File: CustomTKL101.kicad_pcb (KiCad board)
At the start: 2 copper layers, 422.3 x 131.8 mm, 223 parts, among them J1 USB4085-GF-A_REVA, SW1 SW_Push, U1 ATmega32U4-AU, Y1 16MHz

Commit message: tracing re-done
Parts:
- SW1: moved to B.Cu
- moved C5 14.6 mm to (109.0, 97.5), turned to 180 degrees
- moved R1 14.3 mm to (93.1, 85.0), turned to 90 degrees
- moved SW1 13.0 mm to (87.0, 87.1)
- moved C6 12.9 mm to (112.1, 84.5), turned to 90 degrees
- moved C4 10.2 mm to (93.7, 87.9), turned to 180 degrees
- moved R7 6.57 mm to (93.7, 92.8)
- moved R8 6.57 mm to (93.7, 94.9)
- moved R9 3.64 mm to (112.0, 96.8)
- moved C3 1.78 mm to (93.7, 90.2), turned to 180 degrees
- moved U1 1.71 mm to (104.0, 89.4)
- moved C7 1.62 mm to (98.9, 97.5)
- moved R5 0.89 mm to (80.3, 79.4)
- moved F1 0.89 mm to (84.8, 80.0)
- moved R2 0.89 mm to (87.9, 78.6)
- moved R3 0.89 mm to (82.4, 79.4)
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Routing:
- net +5V: track 38.4 -> 107.8 mm, vias 2 -> 5
- net GND: track 121.7 -> 133.8 mm, vias 3 -> 4
- net D-: track 14.2 -> 24.5 mm
- net D+: track 11.9 -> 22.1 mm
- net Net-(R1-Pad2): track 29.3 -> 22.4 mm, vias 2 -> 0
- net Net-(R7-Pad1): track 8.71 -> 4.41 mm
- net Net-(C2-Pad1): track 12.9 -> 9.58 mm, vias 2 -> 0
- net Net-(R8-Pad1): track 7.87 -> 5.17 mm
- net Net-(R9-Pad2): track 2.74 -> 3.97 mm
- net Net-(C1-Pad1): track 6.07 -> 7.06 mm
- net Net-(F1-Pad1): track 12.2 -> 11.6 mm

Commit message: changed numenter footprint
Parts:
- K_87: footprint MX_Alps_Hybrid:MX-1U-NoLED -> MX_Alps_Hybrid:MX-2U-ReversedStabilizers-NoLED
- moved D_87 12.1 mm to (479.4, 187.1), turned to 0 degrees
- turned K_87 to 270 degrees
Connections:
- K_87 pad 1: col21 -> (no net)
- K_87 pad 2: Net-(D_87-Pad2) -> (no net)

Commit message: Board Complete
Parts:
- removed K_0: KEYSW, MX_Alps_Hybrid:MX-1U-NoLED
- removed R2: 1.5k, Resistor_SMD:R_0805_2012Metric
- added MX1: MX-NoLED, MX_Alps_Hybrid:MX-1U-NoLED, F.Cu at (126.9, 83.3)
- D1: renamed from D_0; value D -> D_Small
- D10: renamed from D_9; value D -> D_Small
- D100: renamed from D_100; value D -> D_Small
- D101: renamed from D_87; value D -> D_Small
- D11: renamed from D_10; value D -> D_Small
- D12: renamed from D_11; value D -> D_Small
- D13: renamed from D_12; value D -> D_Small
- D14: renamed from D_13; value D -> D_Small
- D15: renamed from D_14; value D -> D_Small
- D16: renamed from D_15; value D -> D_Small
- D17: renamed from D_16; value D -> D_Small
- D18: renamed from D_17; value D -> D_Small
- D19: renamed from D_18; value D -> D_Small
- D2: renamed from D_1; value D -> D_Small
- D20: renamed from D_19; value D -> D_Small
- D21: renamed from D_20; value D -> D_Small
- D22: renamed from D_21; value D -> D_Small
- D23: renamed from D_22; value D -> D_Small
- D24: renamed from D_23; value D -> D_Small
- D25: renamed from D_24; value D -> D_Small
- D26: renamed from D_25; value D -> D_Small
- D27: renamed from D_26; value D -> D_Small
- D28: renamed from D_27; value D -> D_Small
- D29: renamed from D_28; value D -> D_Small
- D3: renamed from D_2; value D -> D_Small
- D30: renamed from D_29; value D -> D_Small
- D31: renamed from D_30; value D -> D_Small
- D32: renamed from D_31; value D -> D_Small
- D33: renamed from D_32; value D -> D_Small
- D34: renamed from D_33; value D -> D_Small
- D35: renamed from D_34; value D -> D_Small
- D36: renamed from D_35; value D -> D_Small
- D37: renamed from D_36; value D -> D_Small
- D38: renamed from D_37; value D -> D_Small
- D39: renamed from D_38; value D -> D_Small
- D4: renamed from D_3; value D -> D_Small
- D40: renamed from D_39; value D -> D_Small
- D41: renamed from D_40; value D -> D_Small
- D42: renamed from D_41; value D -> D_Small
- D43: renamed from D_42; value D -> D_Small
- D44: renamed from D_43; value D -> D_Small
- D45: renamed from D_44; value D -> D_Small
- D46: renamed from D_45; value D -> D_Small
- D47: renamed from D_46; value D -> D_Small
- D48: renamed from D_47; value D -> D_Small
- D49: renamed from D_48; value D -> D_Small
- D5: renamed from D_4; value D -> D_Small
- D50: renamed from D_49; value D -> D_Small
- D51: renamed from D_50; value D -> D_Small
- D52: renamed from D_51; value D -> D_Small
- D53: renamed from D_52; value D -> D_Small
- D54: renamed from D_53; value D -> D_Small
- D55: renamed from D_54; value D -> D_Small
- D56: renamed from D_55; value D -> D_Small
- D57: renamed from D_56; value D -> D_Small
- D58: renamed from D_57; value D -> D_Small
- D59: renamed from D_58; value D -> D_Small
- D6: renamed from D_5; value D -> D_Small
- D60: renamed from D_59; value D -> D_Small
- D61: renamed from D_60; value D -> D_Small
- D62: renamed from D_61; value D -> D_Small
- D63: renamed from D_62; value D -> D_Small
- D64: renamed from D_63; value D -> D_Small
- D65: renamed from D_64; value D -> D_Small
- D66: renamed from D_65; value D -> D_Small
- D67: renamed from D_66; value D -> D_Small
- D68: renamed from D_67; value D -> D_Small
- D69: renamed from D_68; value D -> D_Small
- D7: renamed from D_6; value D -> D_Small
- D70: renamed from D_69; value D -> D_Small
- D71: renamed from D_70; value D -> D_Small
- D72: renamed from D_71; value D -> D_Small
- D73: renamed from D_72; value D -> D_Small
- D74: renamed from D_73; value D -> D_Small
- D75: renamed from D_74; value D -> D_Small
- D76: renamed from D_75; value D -> D_Small
- D77: renamed from D_76; value D -> D_Small
- D78: renamed from D_77; value D -> D_Small
- D79: renamed from D_78; value D -> D_Small
- D8: renamed from D_7; value D -> D_Small
- D80: renamed from D_79; value D -> D_Small
- D81: renamed from D_80; value D -> D_Small
- D82: renamed from D_81; value D -> D_Small
- D83: renamed from D_82; value D -> D_Small
- D84: renamed from D_83; value D -> D_Small
- D85: renamed from D_84; value D -> D_Small
- D86: renamed from D_85; value D -> D_Small
- D87: renamed from D_86; value D -> D_Small
- D88: renamed from D_88; value D -> D_Small
- D89: renamed from D_89; value D -> D_Small
- D9: renamed from D_8; value D -> D_Small
- D90: renamed from D_90; value D -> D_Small
- D91: renamed from D_91; value D -> D_Small
- D92: renamed from D_92; value D -> D_Small
- D93: renamed from D_93; value D -> D_Small
- D94: renamed from D_94; value D -> D_Small
- D95: renamed from D_95; value D -> D_Small
- D96: renamed from D_96; value D -> D_Small
- D97: renamed from D_97; value D -> D_Small
- D98: renamed from D_98; value D -> D_Small
- D99: renamed from D_99; value D -> D_Small
- MX10: renamed from K_9; value KEYSW -> MX-NoLED
- MX100: renamed from K_100; value KEYSW -> MX-NoLED
- MX101: renamed from K_87; value KEYSW -> MX-NoLED; footprint MX_Alps_Hybrid:MX-2U-ReversedStabilizers-NoLED -> MX_Alps_Hybrid:MX-1U-NoLED
- MX11: renamed from K_10; value KEYSW -> MX-NoLED
- MX12: renamed from K_11; value KEYSW -> MX-NoLED
- MX13: renamed from K_12; value KEYSW -> MX-NoLED
- MX14: renamed from K_13; value KEYSW -> MX-NoLED
- MX15: renamed from K_14; value KEYSW -> MX-NoLED
- MX16: renamed from K_15; value KEYSW -> MX-NoLED
- MX17: renamed from K_16; value KEYSW -> MX-NoLED
- MX18: renamed from K_17; value KEYSW -> MX-NoLED
- MX19: renamed from K_18; value KEYSW -> MX-NoLED
- MX2: renamed from K_1; value KEYSW -> MX-NoLED
- MX20: renamed from K_19; value KEYSW -> MX-NoLED
- MX21: renamed from K_20; value KEYSW -> MX-NoLED
- MX22: renamed from K_21; value KEYSW -> MX-NoLED
- MX23: renamed from K_22; value KEYSW -> MX-NoLED
- MX24: renamed from K_23; value KEYSW -> MX-NoLED
- MX25: renamed from K_24; value KEYSW -> MX-NoLED
- MX26: renamed from K_25; value KEYSW -> MX-NoLED
- MX27: renamed from K_26; value KEYSW -> MX-NoLED
- MX28: renamed from K_27; value KEYSW -> MX-NoLED
- MX29: renamed from K_28; value KEYSW -> MX-NoLED
- MX3: renamed from K_2; value KEYSW -> MX-NoLED
- MX30: renamed from K_29; value KEYSW -> MX-NoLED
- MX31: renamed from K_30; value KEYSW -> MX-NoLED
- MX32: renamed from K_31; value KEYSW -> MX-NoLED; footprint MX_Alps_Hybrid:MX-2U-NoLED -> MX_Alps_Hybrid:MX-1U-NoLED
- MX33: renamed from K_32; value KEYSW -> MX-NoLED
- MX34: renamed from K_33; value KEYSW -> MX-NoLED
- MX35: renamed from K_34; value KEYSW -> MX-NoLED
- MX36: renamed from K_35; value KEYSW -> MX-NoLED
- MX37: renamed from K_36; value KEYSW -> MX-NoLED
- MX38: renamed from K_37; value KEYSW -> MX-NoLED
- MX39: renamed from K_38; value KEYSW -> MX-NoLED; footprint MX_Alps_Hybrid:MX-1.5U-NoLED -> MX_Alps_Hybrid:MX-1U-NoLED
- MX4: renamed from K_3; value KEYSW -> MX-NoLED
- MX40: renamed from K_39; value KEYSW -> MX-NoLED
- MX41: renamed from K_40; value KEYSW -> MX-NoLED
- MX42: renamed from K_41; value KEYSW -> MX-NoLED
- MX43: renamed from K_42; value KEYSW -> MX-NoLED
- MX44: renamed from K_43; value KEYSW -> MX-NoLED
- MX45: renamed from K_44; value KEYSW -> MX-NoLED
- MX46: renamed from K_45; value KEYSW -> MX-NoLED
- MX47: renamed from K_46; value KEYSW -> MX-NoLED
- MX48: renamed from K_47; value KEYSW -> MX-NoLED
- MX49: renamed from K_48; value KEYSW -> MX-NoLED
- MX5: renamed from K_4; value KEYSW -> MX-NoLED
- MX50: renamed from K_49; value KEYSW -> MX-NoLED
- MX51: renamed from K_50; value KEYSW -> MX-NoLED
- MX52: renamed from K_51; value KEYSW -> MX-NoLED; footprint MX_Alps_Hybrid:MX-1.5U-NoLED -> MX_Alps_Hybrid:MX-1U-NoLED
- MX53: renamed from K_52; value KEYSW -> MX-NoLED
- MX54: renamed from K_53; value KEYSW -> MX-NoLED
- MX55: renamed from K_54; value KEYSW -> MX-NoLED
- MX56: renamed from K_55; value KEYSW -> MX-NoLED
- MX57: renamed from K_56; value KEYSW -> MX-NoLED
- MX58: renamed from K_57; value KEYSW -> MX-NoLED
- MX59: renamed from K_58; value KEYSW -> MX-NoLED; footprint MX_Alps_Hybrid:MX-1.75U-NoLED -> MX_Alps_Hybrid:MX-1U-NoLED
- MX6: renamed from K_5; value KEYSW -> MX-NoLED
- MX60: renamed from K_59; value KEYSW -> MX-NoLED
- MX61: renamed from K_60; value KEYSW -> MX-NoLED
- MX62: renamed from K_61; value KEYSW -> MX-NoLED
- MX63: renamed from K_62; value KEYSW -> MX-NoLED
- MX64: renamed from K_63; value KEYSW -> MX-NoLED
- MX65: renamed from K_64; value KEYSW -> MX-NoLED
- MX66: renamed from K_65; value KEYSW -> MX-NoLED
- MX67: renamed from K_66; value KEYSW -> MX-NoLED
- MX68: renamed from K_67; value KEYSW -> MX-NoLED
- MX69: renamed from K_68; value KEYSW -> MX-NoLED
- MX7: renamed from K_6; value KEYSW -> MX-NoLED
- MX70: renamed from K_69; value KEYSW -> MX-NoLED
- MX71: renamed from K_70; value KEYSW -> MX-NoLED; footprint MX_Alps_Hybrid:MX-2.25U-NoLED -> MX_Alps_Hybrid:MX-1U-NoLED
- MX72: renamed from K_71; value KEYSW -> MX-NoLED
- MX73: renamed from K_72; value KEYSW -> MX-NoLED
- MX74: renamed from K_73; value KEYSW -> MX-NoLED
- MX75: renamed from K_74; value KEYSW -> MX-NoLED; footprint MX_Alps_Hybrid:MX-2.25U-NoLED -> MX_Alps_Hybrid:MX-1U-NoLED
- MX76: renamed from K_75; value KEYSW -> MX-NoLED
- MX77: renamed from K_76; value KEYSW -> MX-NoLED
- MX78: renamed from K_77; value KEYSW -> MX-NoLED
- MX79: renamed from K_78; value KEYSW -> MX-NoLED
- MX8: renamed from K_7; value KEYSW -> MX-NoLED
- MX80: renamed from K_79; value KEYSW -> MX-NoLED
- MX81: renamed from K_80; value KEYSW -> MX-NoLED
- MX82: renamed from K_81; value KEYSW -> MX-NoLED
- MX83: renamed from K_82; value KEYSW -> MX-NoLED
- MX84: renamed from K_83; value KEYSW -> MX-NoLED
- MX85: renamed from K_84; value KEYSW -> MX-NoLED
- MX86: renamed from K_85; value KEYSW -> MX-NoLED; footprint MX_Alps_Hybrid:MX-2.75U-NoLED -> MX_Alps_Hybrid:MX-1U-NoLED
- MX87: renamed from K_86; value KEYSW -> MX-NoLED
- MX88: renamed from K_88; value KEYSW -> MX-NoLED
- MX89: renamed from K_89; value KEYSW -> MX-NoLED
- MX9: renamed from K_8; value KEYSW -> MX-NoLED
- MX90: renamed from K_90; value KEYSW -> MX-NoLED; footprint MX_Alps_Hybrid:MX-1.25U-NoLED -> MX_Alps_Hybrid:MX-1U-NoLED
- MX91: renamed from K_91; value KEYSW -> MX-NoLED; footprint MX_Alps_Hybrid:MX-1.25U-NoLED -> MX_Alps_Hybrid:MX-1U-NoLED
- MX92: renamed from K_92; value KEYSW -> MX-NoLED; footprint MX_Alps_Hybrid:MX-1.25U-NoLED -> MX_Alps_Hybrid:MX-1U-NoLED
- MX93: renamed from K_93; value KEYSW -> MX-NoLED; footprint MX_Alps_Hybrid:MX-6.25U-NoLED -> MX_Alps_Hybrid:MX-1U-NoLED
- MX94: renamed from K_94; value KEYSW -> MX-NoLED; footprint MX_Alps_Hybrid:MX-1.25U-NoLED -> MX_Alps_Hybrid:MX-1U-NoLED
- MX95: renamed from K_95; value KEYSW -> MX-NoLED; footprint MX_Alps_Hybrid:MX-1.25U-NoLED -> MX_Alps_Hybrid:MX-1U-NoLED
- MX96: renamed from K_96; value KEYSW -> MX-NoLED; footprint MX_Alps_Hybrid:MX-1.25U-NoLED -> MX_Alps_Hybrid:MX-1U-NoLED
- MX97: renamed from K_97; value KEYSW -> MX-NoLED; footprint MX_Alps_Hybrid:MX-1.25U-NoLED -> MX_Alps_Hybrid:MX-1U-NoLED
- MX98: renamed from K_98; value KEYSW -> MX-NoLED
- MX99: renamed from K_99; value KEYSW -> MX-NoLED
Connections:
- D1 pad 1: row0 -> Row0.1
- D10 pad 1: row0 -> Row0.2
- D100 pad 1: row6 -> Row5.2
- D101 pad 1: row5 -> Row5.1
- D101 pad 2: Net-(D_87-Pad2) -> Net-(D101-Pad2)
- D11 pad 1: row0 -> Row0.1
- D12 pad 1: row0 -> Row0.2
- D13 pad 1: row0 -> Row0.1
- D14 pad 1: row0 -> Row0.2
- D15 pad 1: row0 -> Row0.1
- D16 pad 1: row0 -> Row0.2
- D17 pad 1: row2 -> Row1.1
- D18 pad 1: row2 -> Row1.2
- D19 pad 1: row2 -> Row1.1
- D2 pad 1: row0 -> Row0.1
- D20 pad 1: row2 -> Row1.2
- D21 pad 1: row2 -> Row1.1
- D22 pad 1: row2 -> Row1.2
- D23 pad 1: row2 -> Row1.1
- D24 pad 1: row2 -> Row1.2
- D25 pad 1: row2 -> Row1.1
- D26 pad 1: row2 -> Row1.2
- D27 pad 1: row2 -> Row1.1
- D28 pad 1: row2 -> Row1.2
- D29 pad 1: row2 -> Row1.1
- D3 pad 1: row0 -> Row0.2
- D30 pad 1: row2 -> Row1.2
- D31 pad 1: row2 -> Row1.1
- D32 pad 1: row2 -> Row1.1
- D33 pad 1: row2 -> Row1.2
- D34 pad 1: row2 -> Row1.1
- D35 pad 1: row2 -> Row1.2
- D36 pad 1: row2 -> Row1.1
- D37 pad 1: row3 -> Row2.1
- D38 pad 1: row3 -> Row2.2
- D39 pad 1: row3 -> Row2.2
- D4 pad 1: row0 -> Row0.1
- D40 pad 1: row3 -> Row2.1
- D41 pad 1: row3 -> Row2.2
- D42 pad 1: row3 -> Row2.1
- D43 pad 1: row3 -> Row2.2
- D44 pad 1: row3 -> Row2.1
- D45 pad 1: row3 -> Row2.2
- D46 pad 1: row3 -> Row2.1
- D47 pad 1: row3 -> Row2.2
- D48 pad 1: row3 -> Row2.1
- D49 pad 1: row3 -> Row2.2
- D5 pad 1: row0 -> Row0.2
- D50 pad 1: row3 -> Row2.1
- D51 pad 1: row3 -> Row2.2
- D52 pad 1: row3 -> Row2.1
- D53 pad 1: row3 -> Row2.2
- D54 pad 1: row3 -> Row2.1
- D55 pad 1: row3 -> Row2.2
- D56 pad 1: row3 -> Row2.1
- D57 pad 1: row4 -> Row3.1
- D58 pad 1: row4 -> Row3.2
- D59 pad 1: row4 -> Row3.2
- D6 pad 1: row0 -> Row0.1
- D60 pad 1: row4 -> Row3.1
- D61 pad 1: row4 -> Row3.2
- D62 pad 1: row4 -> Row3.1
- D63 pad 1: row4 -> Row3.2
- D64 pad 1: row4 -> Row3.1
- D65 pad 1: row4 -> Row3.2
- D66 pad 1: row4 -> Row3.1
- D67 pad 1: row4 -> Row3.2
- D68 pad 1: row4 -> Row3.1
- D69 pad 1: row4 -> Row3.2
- D7 pad 1: row0 -> Row0.2
- D70 pad 1: row4 -> Row3.1
- D71 pad 1: row4 -> Row3.1
- D72 pad 1: row4 -> Row3.1
- D73 pad 1: row5 -> Row4.1
- D74 pad 1: row5 -> Row4.2
- D75 pad 1: row5 -> Row4.2
- D76 pad 1: row5 -> Row4.2
- D77 pad 1: row5 -> Row4.1
- D78 pad 1: row5 -> Row4.2
- D79 pad 1: row5 -> Row4.1
- D8 pad 1: row0 -> Row0.1
- D80 pad 1: row5 -> Row4.2
- D81 pad 1: row5 -> Row4.1
- D82 pad 1: row5 -> Row4.2
- D83 pad 1: row5 -> Row4.1
- D84 pad 1: row5 -> Row4.2
- D85 pad 1: row5 -> Row4.1
- D86 pad 1: row5 -> Row4.2
- D87 pad 1: row5 -> Row4.1
- D88 pad 1: row6 -> Row5.1
- D89 pad 1: row6 -> Row5.2
- D9 pad 1: row0 -> Row0.2
- D90 pad 1: row6 -> Row5.1
- D91 pad 1: row6 -> Row5.1
- D92 pad 1: row6 -> Row5.2
- D93 pad 1: row6 -> Row5.2
- D94 pad 1: row6 -> Row5.1
- D95 pad 1: row6 -> Row5.1
- D96 pad 1: row6 -> Row5.2
- D97 pad 1: row6 -> Row5.1
- D98 pad 1: row6 -> Row5.2
- D99 pad 1: row6 -> Row5.1
- J1 pad P1: Net-(J1-PadP1) -> GND
- J1 pad P2: Net-(J1-PadP1) -> GND
- J1 pad P3: Net-(J1-PadP1) -> GND
- J1 pad P4: Net-(J1-PadP1) -> GND
- MX10 pad 1: col13 -> Col12&13
- MX100 pad 1: col20 -> Col18&19
- MX101 pad 1: (no net) -> Col20
- MX101 pad 2: (no net) -> Net-(D101-Pad2)
- MX11 pad 1: col14 -> Col14&15
- MX12 pad 1: col15 -> Col14&15
- MX13 pad 1: col16 -> Col16&17
- MX14 pad 1: col18 -> Col16&17
- MX15 pad 1: col19 -> Col18&19
- MX16 pad 1: col20 -> Col18&19
- MX17 pad 1: col0 -> Col0&1
- MX18 pad 1: col1 -> Col0&1
- MX19 pad 1: col2 -> Col2&3
- MX2 pad 1: col4 -> Col4&5
- MX20 pad 1: col3 -> Col2&3
- MX21 pad 1: col4 -> Col4&5
- MX22 pad 1: col5 -> Col4&5
- MX23 pad 1: col6 -> Col6&7
- MX24 pad 1: col7 -> Col6&7
- MX25 pad 1: col8 -> Col8&9
- MX26 pad 1: col9 -> Col8&9
- MX27 pad 1: col10 -> Col10&11
- MX28 pad 1: col11 -> Col10&11
- MX29 pad 1: col12 -> Col12&13
- MX3 pad 1: col5 -> Col4&5
- MX30 pad 1: col13 -> Col12&13
- MX31 pad 1: col14 -> Col14&15
- MX32 pad 1: col16 -> Col16&17
- MX33 pad 1: col18 -> Col16&17
- MX34 pad 1: col19 -> Col18&19
- MX35 pad 1: col20 -> Col18&19
- MX36 pad 1: col21 -> Col20
- MX37 pad 1: col0 -> Col0&1
- MX38 pad 1: col1 -> Col0&1
- MX39 pad 1: col3 -> Col2&3
- MX4 pad 1: col6 -> Col6&7
- MX40 pad 1: col4 -> Col4&5
- MX41 pad 1: col5 -> Col4&5
- MX42 pad 1: col6 -> Col6&7
- MX43 pad 1: col7 -> Col6&7
- MX44 pad 1: col8 -> Col8&9
- MX45 pad 1: col9 -> Col8&9
- MX46 pad 1: col10 -> Col10&11
- MX47 pad 1: col11 -> Col10&11
- MX48 pad 1: col12 -> Col12&13
- MX49 pad 1: col13 -> Col12&13
- MX5 pad 1: col7 -> Col6&7
- MX50 pad 1: col14 -> Col14&15
- MX51 pad 1: col15 -> Col14&15
- MX52 pad 1: col16 -> Col16&17
- MX53 pad 1: col18 -> Col16&17
- MX54 pad 1: col19 -> Col18&19
- MX55 pad 1: col20 -> Col18&19
- MX56 pad 1: col21 -> Col20
- MX57 pad 1: col0 -> Col0&1
- MX58 pad 1: col1 -> Col0&1
- MX59 pad 1: col3 -> Col2&3
- MX6 pad 1: col8 -> Col8&9
- MX60 pad 1: col4 -> Col4&5
- MX61 pad 1: col5 -> Col4&5
- MX62 pad 1: col6 -> Col6&7
- MX63 pad 1: col7 -> Col6&7
- MX64 pad 1: col8 -> Col8&9
- MX65 pad 1: col9 -> Col8&9
- MX66 pad 1: col10 -> Col10&11
- MX67 pad 1: col11 -> Col10&11
- MX68 pad 1: col12 -> Col12&13
- MX69 pad 1: col13 -> Col12&13
- MX7 pad 1: col9 -> Col8&9
- MX70 pad 1: col14 -> Col14&15
- MX71 pad 1: col16 -> Col16&17
- MX72 pad 1: col21 -> Col20
- MX73 pad 1: col0 -> Col0&1
- MX74 pad 1: col1 -> Col0&1
- MX75 pad 1: col3 -> Col2&3
- MX76 pad 1: col5 -> Col4&5
- MX77 pad 1: col6 -> Col6&7
- MX78 pad 1: col7 -> Col6&7
- MX79 pad 1: col8 -> Col8&9
- MX8 pad 1: col10 -> Col10&11
- MX80 pad 1: col9 -> Col8&9
- MX81 pad 1: col10 -> Col10&11
- MX82 pad 1: col11 -> Col10&11
- MX83 pad 1: col12 -> Col12&13
- MX84 pad 1: col13 -> Col12&13
- MX85 pad 1: col14 -> Col14&15
- MX86 pad 1: col15 -> Col14&15
- MX87 pad 1: col19 -> Col18&19
- MX88 pad 1: col0 -> Col0&1
- MX89 pad 1: col1 -> Col0&1
- MX9 pad 1: col11 -> Col10&11
- MX90 pad 1: col2 -> Col2&3
- MX91 pad 1: col4 -> Col4&5
- MX92 pad 1: col5 -> Col4&5
- MX93 pad 1: col9 -> Col8&9
- MX94 pad 1: col12 -> Col12&13
- MX95 pad 1: col14 -> Col14&15
- MX96 pad 1: col15 -> Col14&15
- MX97 pad 1: col16 -> Col16&17
- MX98 pad 1: col18 -> Col16&17
- MX99 pad 1: col19 -> Col18&19
- U1 pad 10: Net-(U1-Pad10) -> Col6&7
- U1 pad 11: Net-(U1-Pad11) -> Col8&9
- U1 pad 12: Net-(U1-Pad12) -> Col10&11
- U1 pad 18: Net-(U1-Pad18) -> Col20
- U1 pad 19: Net-(U1-Pad19) -> Col18&19
- U1 pad 20: Net-(U1-Pad20) -> Col16&17
- U1 pad 21: Net-(U1-Pad21) -> Col14&15
- U1 pad 22: Net-(U1-Pad22) -> Col12&13
- U1 pad 25: Net-(U1-Pad25) -> Row0.1
- U1 pad 26: Net-(U1-Pad26) -> Row0.2
- U1 pad 28: Net-(U1-Pad28) -> Row5.2
- U1 pad 29: Net-(U1-Pad29) -> Row4.2
- U1 pad 30: Net-(U1-Pad30) -> Row3.2
- U1 pad 31: Net-(U1-Pad31) -> Row2.2
- U1 pad 32: Net-(U1-Pad32) -> Row1.2
- U1 pad 36: Net-(U1-Pad36) -> Row5.1
- U1 pad 37: Net-(U1-Pad37) -> Row4.1
- U1 pad 38: Net-(U1-Pad38) -> Row3.1
- U1 pad 39: Net-(U1-Pad39) -> Row2.1
- U1 pad 40: Net-(U1-Pad40) -> Row1.1
- U1 pad 41: Net-(U1-Pad41) -> Col0&1
- U1 pad 8: Net-(U1-Pad8) -> Col2&3
- U1 pad 9: Net-(U1-Pad9) -> Col4&5
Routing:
- net Col16&17: track 0.00 -> 588.6 mm, vias 0 -> 3
- net Col18&19: track 0.00 -> 582.7 mm, vias 0 -> 1
- net Row5.1: track 0.00 -> 498.7 mm, vias 0 -> 2
- net Col20: track 0.00 -> 485.3 mm, vias 0 -> 1
- net Col14&15: track 0.00 -> 475.8 mm, vias 0 -> 1
- net Row3.1: track 0.00 -> 466.9 mm, vias 0 -> 4
- net Row5.2: track 0.00 -> 459.3 mm, vias 0 -> 9
- net Row2.1: track 0.00 -> 451.3 mm, vias 0 -> 4
- net Row4.1: track 0.00 -> 442.8 mm, vias 0 -> 4
- net Col12&13: track 0.00 -> 436.9 mm, vias 0 -> 3
- net Row1.1: track 0.00 -> 429.5 mm, vias 0 -> 4
- net Col10&11: track 0.00 -> 410.4 mm, vias 0 -> 1
- net Row2.2: track 0.00 -> 404.4 mm, vias 0 -> 24
- net Col8&9: track 0.00 -> 395.3 mm, vias 0 -> 1
- net Row1.2: track 0.00 -> 380.5 mm, vias 0 -> 21
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
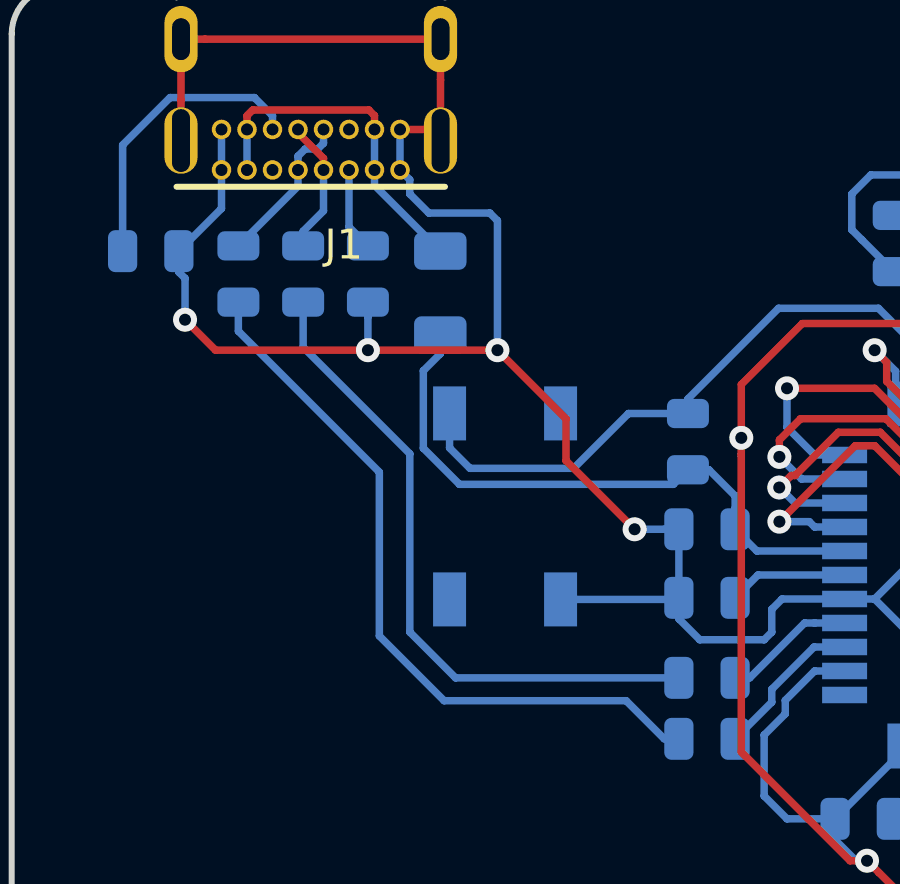
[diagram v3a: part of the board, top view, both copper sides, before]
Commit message: Removed dataline resistors
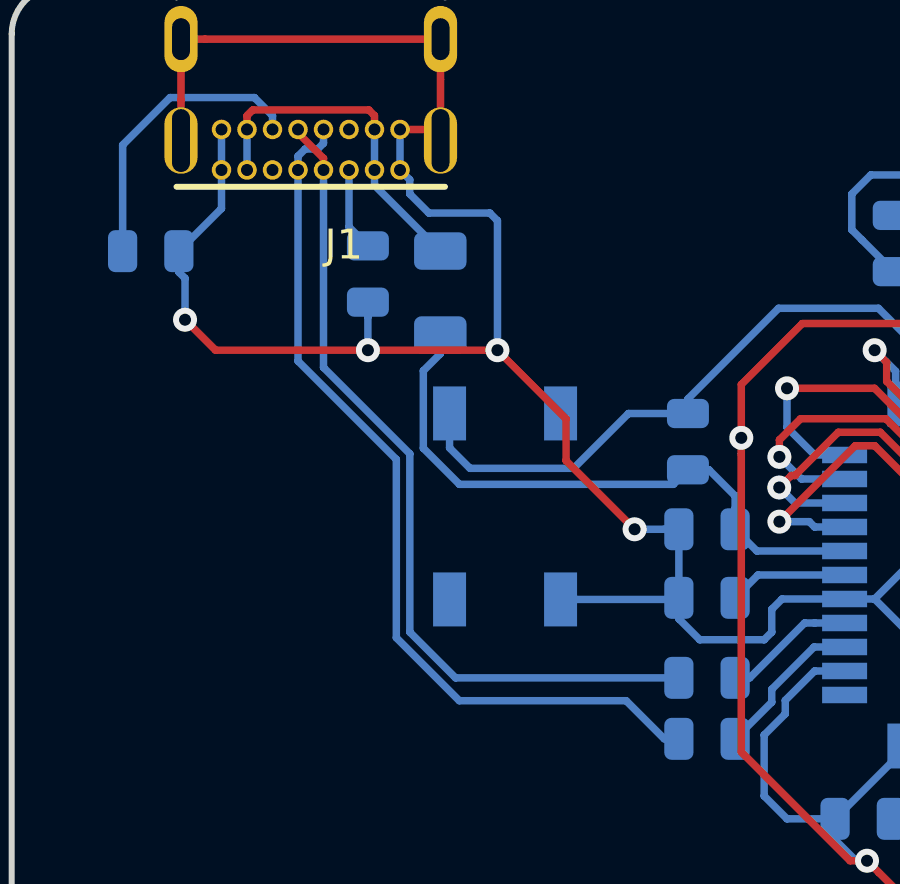
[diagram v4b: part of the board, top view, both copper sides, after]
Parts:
- removed R5, R6: 5.1kohm, Resistor_SMD:R_0805_2012Metric
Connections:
- J1 pad A6: Net-(J1-PadA6) -> D+
- J1 pad A7: Net-(J1-PadA7) -> D-
- J1 pad B6: Net-(J1-PadA6) -> D+
- J1 pad B7: Net-(J1-PadA7) -> D-
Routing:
- net D+: track 22.1 -> 27.9 mm
- net Net-(J1-PadA7): track 5.30 -> 0.00 mm
- net D-: track 24.5 -> 29.7 mm
- net Net-(J1-PadA6): track 4.51 -> 0.00 mm

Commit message: routing fixing
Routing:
- net +5V: track 105.0 -> 106.9 mm
- net GND: track 147.8 -> 148.8 mm
